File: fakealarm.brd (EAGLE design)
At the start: 34.5 x 34.5 mm, 14 parts, among them IC1 NE555N, Q1 2N3904, X1 RUN, X2 BAT, X3 GND

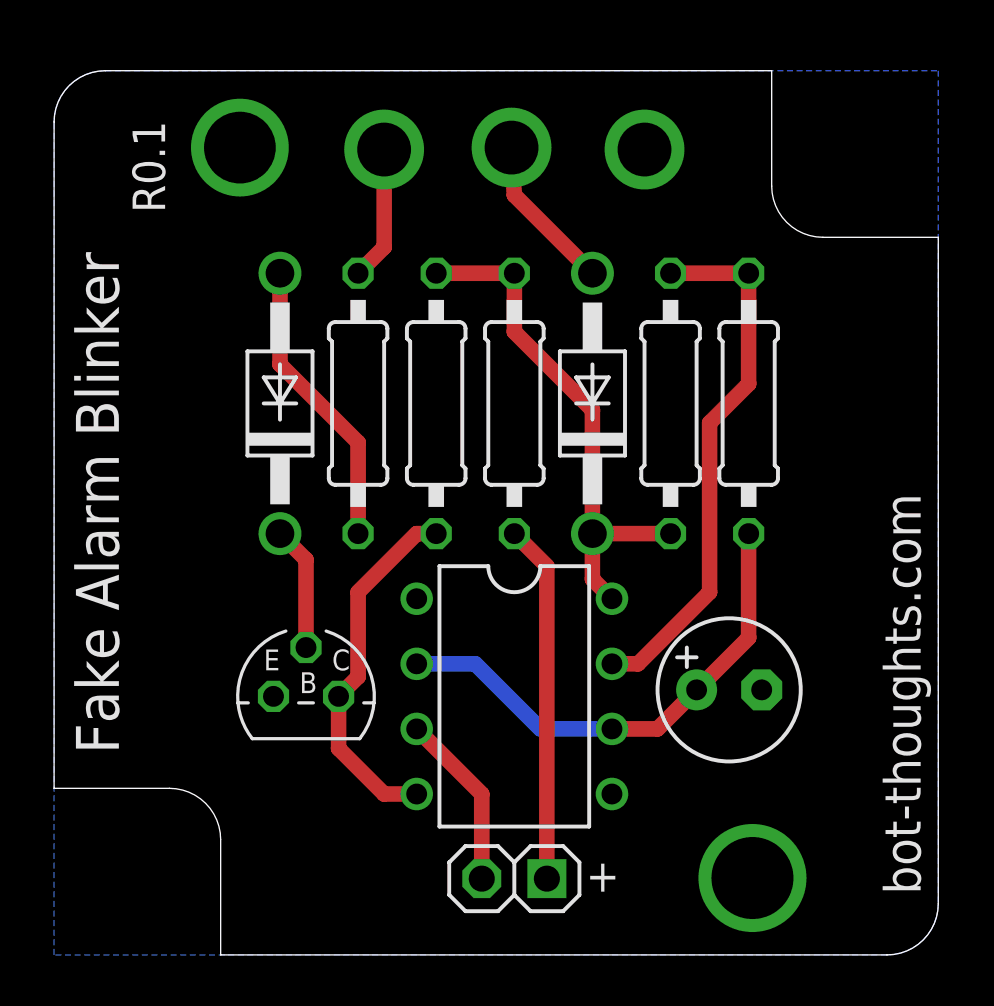
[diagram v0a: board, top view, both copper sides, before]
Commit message: Added 10nF (0.01uF) bypass on CV, shrank board, moved components around a little
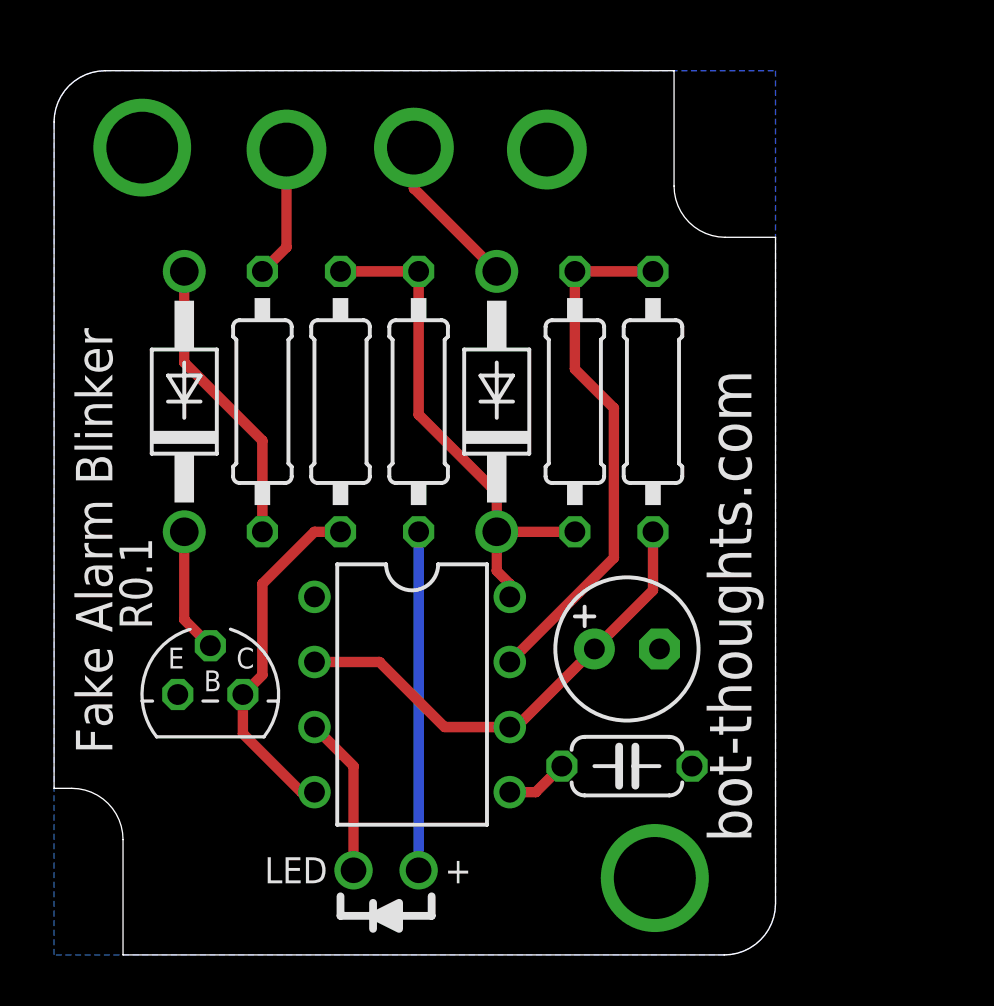
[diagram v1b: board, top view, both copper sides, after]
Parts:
- removed JP1: LED, pinhead-2:1X02-S
- added C2: 103, rcl:C050-024X044
- added X4: +, bt_electromech:PAD_24GA
- added X5: LED, bt_electromech:PAD_24GA
- moved C1 4.30 mm to (22.4, 11.9)
- moved IC1 3.99 mm to (14.0, 10.2)
- moved X2 3.81 mm to (14.0, 31.5)
- moved X1 3.81 mm to (9.07, 31.4)
- moved X3 3.81 mm to (19.2, 31.4)
- moved D2 3.73 mm to (17.3, 21.6)
- moved R2 3.73 mm to (23.4, 21.6)
- moved D1 3.73 mm to (5.08, 21.6)
- moved Q1 3.73 mm to (6.10, 10.2)
- moved R3 3.73 mm to (8.13, 21.6)
- moved R4 3.73 mm to (11.2, 21.6)
- moved R1 3.73 mm to (20.3, 21.6)
- moved R5 3.73 mm to (14.2, 21.6)
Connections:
- new net N$7: C2.1, IC1.5
- net GND: now also C2.2
- net N$10: now also X5.P$1; no longer JP1.2
- net N$9: now also X4.P$1; no longer JP1.1
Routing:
- net N$7: track 0.00 -> 2.45 mm
- net N$4: track 19.5 -> 18.8 mm
- net N$9: track 14.0 -> 13.2 mm
- net N$10: track 6.89 -> 6.22 mm
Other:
- board size 34.5 x 34.5 mm -> 28.1 x 34.5 mm
- board text removed: "+"

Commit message: added oshw logo, minor silk layout tweaks
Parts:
- added LOGO1: OSHW-LOGOS, SparkFun-Aesthetics:OSHW-LOGO-S
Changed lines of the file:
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@@
 <wire x1="2" y1="34.5" x2="0" y2="32.5" width="0" layer="20" curve="90"/>
 <wire x1="0" y1="32.5" x2="0" y2="6.5" width="0" layer="20"/>
-<text x="2.274" y="7.848" size="1.4224" layer="25" font="vector" ratio="12" rot="R90">Fake Alarm Blinker</text>
+<text x="2.02" y="8.102" size="1.4224" layer="25" font="vector" ratio="12" rot="R90">Fake Alarm Blinker</text>
 <text x="27.208" y="4.396" size="1.6764" layer="25" font="vector" ratio="12" rot="R90">bot-thoughts.com</text>
-<text x="3.824" y="12.704" size="1.27" layer="25" font="vector" ratio="12" rot="R90">R0.1</text>
+<text x="23.636" y="30.23" size="1.27" layer="25" font="vector" ratio="12" rot="R90">R0.1</text>
 <text x="4.054" y="35.6" size="1.27" layer="48" font="vector" ratio="12">For Hammond 1551Q</text>
 <wire x1="24.19" y1="34.5" x2="24.19" y2="30" width="0" layer="20"/>
@@
 <elements>
 <element name="C1" library="rcl" package="E2,5-6" value="33uF" x="22.352" y="11.938" smashed="yes">
-<attribute name="VALUE" x="19.685" y="10.668" size="1.016" layer="28" font="vector" ratio="10" rot="MR180"/>
+<attribute name="VALUE" x="20.447" y="10.414" size="1.016" layer="28" font="vector" ratio="10" rot="MR180"/>
 <attribute name="VOLTAGE" value="25V" x="22.352" y="11.938" size="1.778" layer="27" display="off"/>
 </element>
@@
 </element>
 <element name="X4" library="bt_electromech" package="PAD_24GA" value="+" x="14.224" y="3.302" smashed="yes">
-<attribute name="VALUE" x="15.24" y="2.794" size="1.016" layer="21" font="vector"/>
+<attribute name="VALUE" x="15.494" y="2.54" size="1.6764" layer="21" font="vector"/>
 </element>
 <element name="X5" library="bt_electromech" package="PAD_24GA" value="LED" x="11.684" y="3.302" smashed="yes" rot="R180">
-<attribute name="VALUE" x="10.668" y="3.81" size="1.016" layer="21" font="vector" rot="R180"/>
+<attribute name="VALUE" x="10.414" y="3.81" size="1.016" layer="21" font="vector" rot="R180"/>
 </element>
 <element name="C2" library="rcl" package="C050-024X044" value="103" x="22.352" y="7.366" smashed="yes">
 <attribute name="VALUE" x="23.495" y="6.731" size="1.016" layer="28" font="vector" ratio="10" rot="MR0"/>
 </element>
+<element name="LOGO1" library="SparkFun-Aesthetics" package="OSHW-LOGO-S" value="OSHW-LOGOS" x="19.304" y="3.302" rot="R90"/>
 </elements>
 <signals>

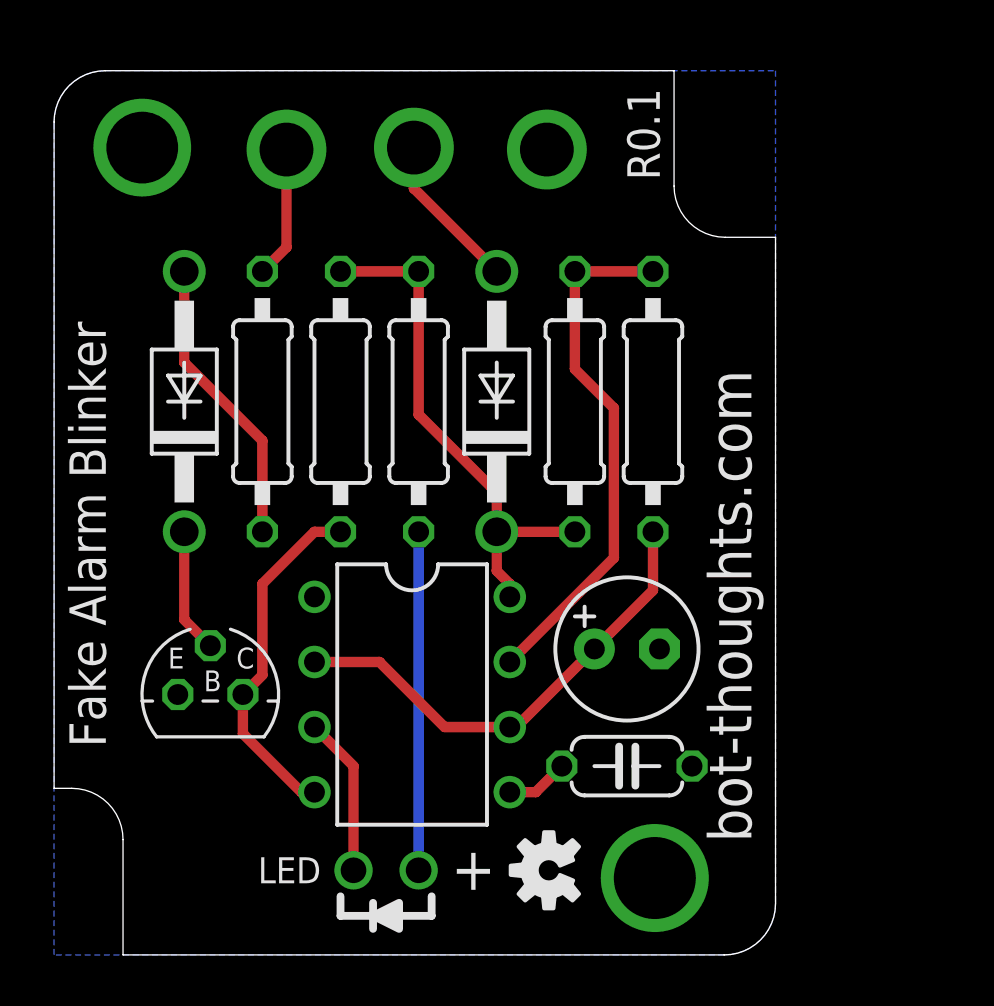
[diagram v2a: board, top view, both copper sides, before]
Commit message: Generated silk, added enclosure info to schematic
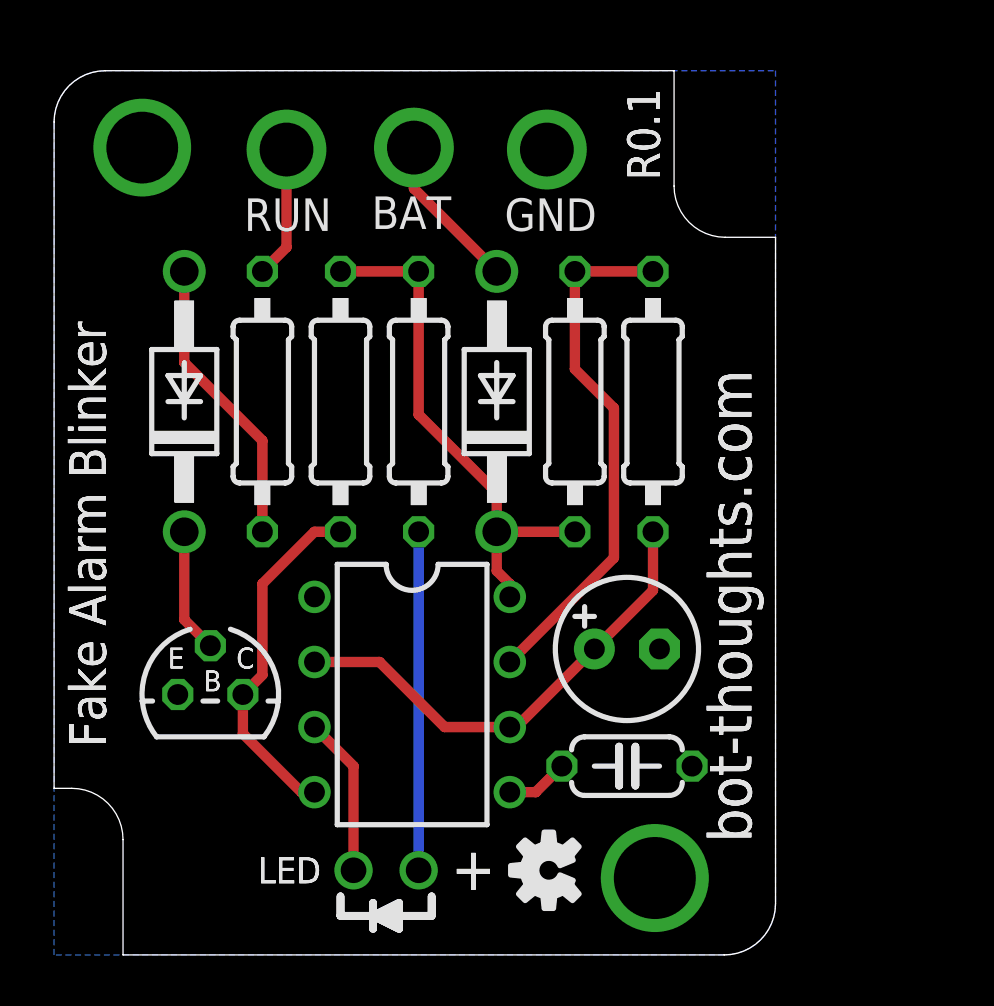
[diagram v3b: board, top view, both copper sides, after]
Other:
- board text added: "+"
- board text added: "100K"
- board text added: "103"
- board text added: "10k"
- board text added: "1K"
- board text added: "1N4004"
- board text added: "2N3904"
- board text added: "33k"
- board text added: "33uF"
- board text added: "B"
- board text added: "BAT"
- board text added: "C"
- board text added: "E"
- board text added: "GND"
- board text added: "LED"
- board text added: "NE555N"
- board text added: "RUN"
